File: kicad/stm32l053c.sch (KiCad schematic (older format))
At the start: 29 parts, among them P1 SWD, P2 PWR, Q1 Q_NMOS_GSD, SW1 SW_PUSH, SW2 SW_PUSH, SW3 SW_PUSH, U1 STM32L053C8_LQFP48, U2 TLV61225, Y1 Crystal

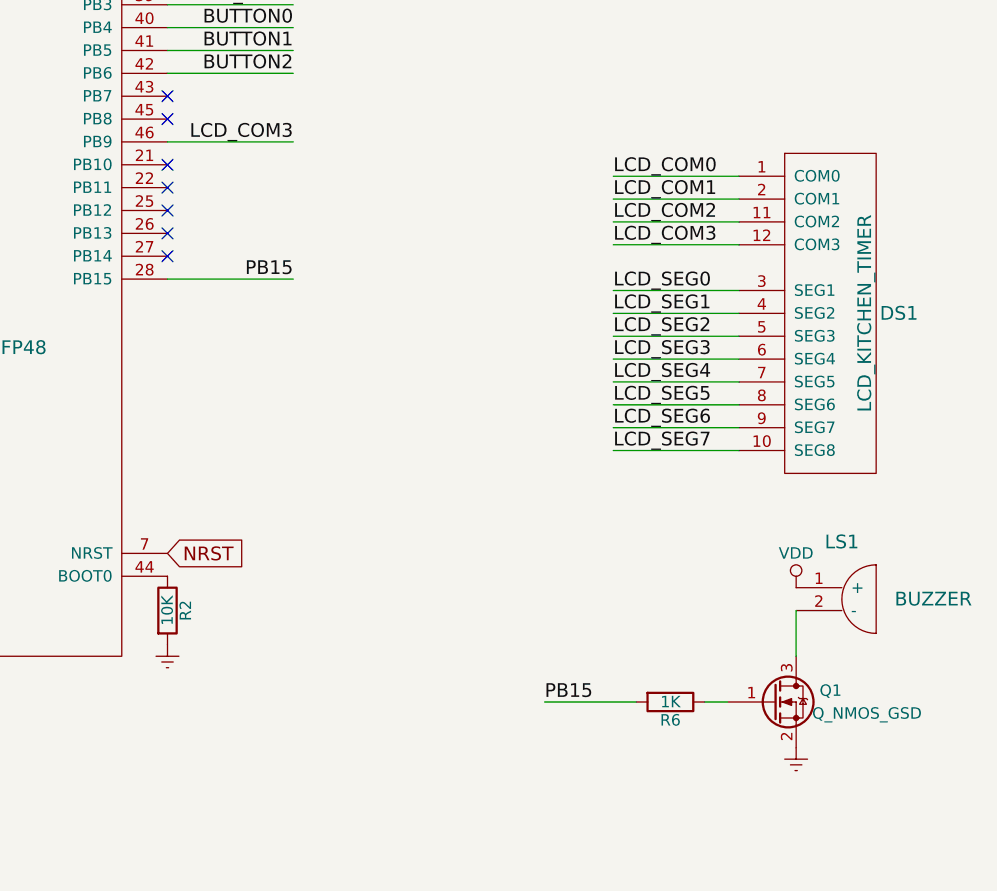
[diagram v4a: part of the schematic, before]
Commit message: 62 ms pulses of 2048Hz for the buzzer alarm
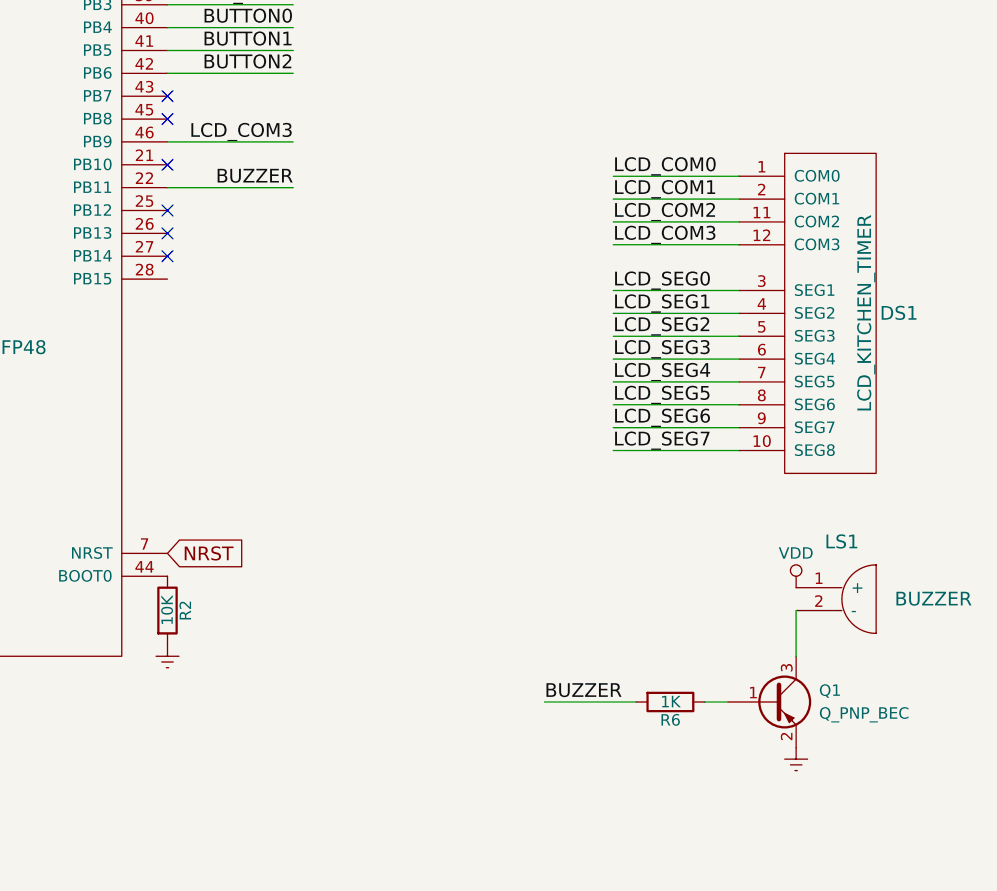
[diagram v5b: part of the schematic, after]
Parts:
- removed Q1: Q_NMOS_GSD, TO_SOT_Packages_SMD:SOT-23_Handsoldering, symbol Q_NMOS_GSD
- added Q1: Q_PNP_BEC, symbol Q_PNP_BEC
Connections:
- net Earth: now also Q1.2 (E)
- net BUZZER: now reaches U1.22 (PB11)
- net BUZZER: now also R6.2
- net at LS1.2 (-): now also Q1.3 (C)
- net at R6.1: now also Q1.1 (B)
- net PB15: no longer names the net of U1.28 (PB15)
- net PB15: no longer R6.2
- no-connect marks 15 -> 14
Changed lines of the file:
@@
 $EndDescr
 $Comp
-L Earth #PWR01
+L Earth #PWR27
 U 1 1 58021BE1
 P 4900 7200
-F 0 "#PWR01" H 4900 6950 50  0001 C CNN
+F 0 "#PWR27" H 4900 6950 50  0001 C CNN
 F 1 "Earth" H 4900 7050 50  0001 C CNN
 F 2 "" H 4900 7200 50  0000 C CNN
@@
 $EndComp
 $Comp
-L VDD #PWR02
+L VDD #PWR25
 U 1 1 58021C2A
 P 4900 6900
-F 0 "#PWR02" H 4900 6750 50  0001 C CNN
+F 0 "#PWR25" H 4900 6750 50  0001 C CNN
 F 1 "VDD" H 4900 7050 50  0000 C CNN
 F 2 "" H 4900 6900 50  0000 C CNN
@@
 $EndComp
 $Comp
-L GNDA #PWR03
+L GNDA #PWR19
 U 1 1 58021F75
 P 5100 6300
-F 0 "#PWR03" H 5100 6050 50  0001 C CNN
+F 0 "#PWR19" H 5100 6050 50  0001 C CNN
 F 1 "GNDA" H 5100 6150 50  0000 C CNN
 F 2 "" H 5100 6300 50  0000 C CNN
@@
 $EndComp
 $Comp
-L Earth #PWR04
+L Earth #PWR20
 U 1 1 58021F89
 P 5600 6300
-F 0 "#PWR04" H 5600 6050 50  0001 C CNN
+F 0 "#PWR20" H 5600 6050 50  0001 C CNN
 F 1 "Earth" H 5600 6150 50  0001 C CNN
 F 2 "" H 5600 6300 50  0000 C CNN
@@
 $EndComp
 $Comp
-L GNDA #PWR05
+L GNDA #PWR16
 U 1 1 58022154
 P 5150 5800
-F 0 "#PWR05" H 5150 5550 50  0001 C CNN
+F 0 "#PWR16" H 5150 5550 50  0001 C CNN
 F 1 "GNDA" H 5150 5650 50  0000 C CNN
 F 2 "" H 5150 5800 50  0000 C CNN
@@
 $EndComp
 $Comp
-L Earth #PWR06
+L Earth #PWR17
 U 1 1 580221FA
 P 5650 5800
-F 0 "#PWR06" H 5650 5550 50  0001 C CNN
+F 0 "#PWR17" H 5650 5550 50  0001 C CNN
 F 1 "Earth" H 5650 5650 50  0001 C CNN
 F 2 "" H 5650 5800 50  0000 C CNN
@@
 $EndComp
 $Comp
-L VDD #PWR07
+L VDD #PWR1
 U 1 1 5802295B
 P 5450 1050
-F 0 "#PWR07" H 5450 900 50  0001 C CNN
+F 0 "#PWR1" H 5450 900 50  0001 C CNN
 F 1 "VDD" H 5450 1200 50  0000 C CNN
 F 2 "" H 5450 1050 50  0000 C CNN
@@
 $EndComp
 $Comp
-L Earth #PWR08
+L Earth #PWR4
 U 1 1 5803310F
 P 4800 1800
-F 0 "#PWR08" H 4800 1550 50  0001 C CNN
+F 0 "#PWR4" H 4800 1550 50  0001 C CNN
 F 1 "Earth" H 4800 1650 50  0001 C CNN
 F 2 "" H 4800 1800 50  0000 C CNN
@@
 $EndComp
 $Comp
-L Earth #PWR09
+L Earth #PWR3
 U 1 1 580369A9
 P 2150 1400
-F 0 "#PWR09" H 2150 1150 50  0001 C CNN
+F 0 "#PWR3" H 2150 1150 50  0001 C CNN
 F 1 "Earth" H 2150 1250 50  0001 C CNN
 F 2 "" H 2150 1400 50  0000 C CNN
@@
 NRST
 $Comp
-L VDD #PWR010
+L VDD #PWR2
 U 1 1 5803734F
 P 1650 1200
-F 0 "#PWR010" H 1650 1050 50  0001 C CNN
+F 0 "#PWR2" H 1650 1050 50  0001 C CNN
 F 1 "VDD" H 1650 1350 50  0000 C CNN
 F 2 "" H 1650 1200 50  0000 C CNN
@@
 $EndComp
 $Comp
-L Earth #PWR011
+L Earth #PWR28
 U 1 1 5803BDC8
 P 5950 7200
-F 0 "#PWR011" H 5950 6950 50  0001 C CNN
+F 0 "#PWR28" H 5950 6950 50  0001 C CNN
 F 1 "Earth" H 5950 7050 50  0001 C CNN
 F 2 "" H 5950 7200 50  0000 C CNN
@@
 $EndComp
 $Comp
-L Earth #PWR012
+L Earth #PWR12
 U 1 1 58065816
 P 6550 5400
-F 0 "#PWR012" H 6550 5150 50  0001 C CNN
+F 0 "#PWR12" H 6550 5150 50  0001 C CNN
 F 1 "Earth" H 6550 5250 50  0001 C CNN
 F 2 "" H 6550 5400 50  0000 C CNN
@@
 $EndComp
 $Comp
-L Earth #PWR013
+L Earth #PWR14
 U 1 1 5806680D
 P 3600 5700
-F 0 "#PWR013" H 3600 5450 50  0001 C CNN
+F 0 "#PWR14" H 3600 5450 50  0001 C CNN
 F 1 "Earth" H 3600 5550 50  0001 C CNN
 F 2 "" H 3600 5700 50  0000 C CNN
@@
 NoConn ~ 6550 3100
 NoConn ~ 6550 3300
-NoConn ~ 6550 3400
 NoConn ~ 6550 3500
 NoConn ~ 6550 3600
@@
 $EndComp
 $Comp
-L +BATT #PWR015
+L +BATT #PWR22
 U 1 1 584F2368
 P 850 6750
-F 0 "#PWR015" H 850 6600 50  0001 C CNN
+F 0 "#PWR22" H 850 6600 50  0001 C CNN
 F 1 "+BATT" H 850 6890 50  0000 C CNN
 F 2 "" H 850 6750 50  0000 C CNN
@@
 Connection ~ 2700 6550
 $Comp
-L Earth #PWR016
+L Earth #PWR24
 U 1 1 584F287E
 P 2850 6850
-F 0 "#PWR016" H 2850 6600 50  0001 C CNN
+F 0 "#PWR24" H 2850 6600 50  0001 C CNN
 F 1 "Earth" H 2850 6700 50  0001 C CNN
 F 2 "" H 2850 6850 50  0000 C CNN
@@
 $EndComp
 $Comp
-L Earth #PWR017
+L Earth #PWR23
 U 1 1 584F28E3
 P 1700 6850
-F 0 "#PWR017" H 1700 6600 50  0001 C CNN
+F 0 "#PWR23" H 1700 6600 50  0001 C CNN
 F 1 "Earth" H 1700 6700 50  0001 C CNN
 F 2 "" H 1700 6850 50  0000 C CNN
@@
 $EndComp
 $Comp
-L Earth #PWR018
+L Earth #PWR26
 U 1 1 584F2924
 P 1250 7050
-F 0 "#PWR018" H 1250 6800 50  0001 C CNN
+F 0 "#PWR26" H 1250 6800 50  0001 C CNN
 F 1 "Earth" H 1250 6900 50  0001 C CNN
 F 2 "" H 1250 7050 50  0000 C CNN
@@
 $EndComp
 $Comp
-L VDD #PWR019
+L VDD #PWR21
 U 1 1 584F2A51
 P 3700 6400
-F 0 "#PWR019" H 3700 6250 50  0001 C CNN
+F 0 "#PWR21" H 3700 6250 50  0001 C CNN
 F 1 "VDD" H 3700 6550 50  0000 C CNN
 F 2 "" H 3700 6400 50  0000 C CNN
@@
 $EndComp
 $Comp
-L VDD #PWR020
+L VDD #PWR5
 U 1 1 585069C3
 P 1300 2700
-F 0 "#PWR020" H 1300 2550 50  0001 C CNN
+F 0 "#PWR5" H 1300 2550 50  0001 C CNN
 F 1 "VDD" H 1300 2850 50  0000 C CNN
 F 2 "" H 1300 2700 50  0000 C CNN
@@
 $EndComp
 $Comp
-L VDD #PWR021
+L VDD #PWR7
 U 1 1 58506BE4
 P 1300 3300
-F 0 "#PWR021" H 1300 3150 50  0001 C CNN
+F 0 "#PWR7" H 1300 3150 50  0001 C CNN
 F 1 "VDD" H 1300 3450 50  0000 C CNN
 F 2 "" H 1300 3300 50  0000 C CNN
@@
 $EndComp
 $Comp
-L VDD #PWR022
+L VDD #PWR9
 U 1 1 58506C86
 P 1300 3900
-F 0 "#PWR022" H 1300 3750 50  0001 C CNN
+F 0 "#PWR9" H 1300 3750 50  0001 C CNN
 F 1 "VDD" H 1300 4050 50  0000 C CNN
 F 2 "" H 1300 3900 50  0000 C CNN
@@
 	2450 2850 3000 2850
 $Comp
-L Earth #PWR023
+L Earth #PWR6
 U 1 1 5851A35F
 P 2450 3150
-F 0 "#PWR023" H 2450 2900 50  0001 C CNN
+F 0 "#PWR6" H 2450 2900 50  0001 C CNN
 F 1 "Earth" H 2450 3000 50  0001 C CNN
 F 2 "" H 2450 3150 50  0000 C CNN
@@
 $EndComp
 $Comp
-L Earth #PWR024
+L Earth #PWR8
 U 1 1 5851A4F4
 P 2450 3750
-F 0 "#PWR024" H 2450 3500 50  0001 C CNN
+F 0 "#PWR8" H 2450 3500 50  0001 C CNN
 F 1 "Earth" H 2450 3600 50  0001 C CNN
 F 2 "" H 2450 3750 50  0000 C CNN
@@
 $EndComp
 $Comp
-L Earth #PWR025
+L Earth #PWR10
 U 1 1 5851A54D
 P 2450 4350
-F 0 "#PWR025" H 2450 4100 50  0001 C CNN
+F 0 "#PWR10" H 2450 4100 50  0001 C CNN
 F 1 "Earth" H 2450 4200 50  0001 C CNN
 F 2 "" H 2450 4350 50  0000 C CNN
@@
 	8600 5650 8200 5650
 $Comp
-L Earth #PWR026
+L Earth #PWR18
 U 1 1 5851B22D
 P 9300 5850
-F 0 "#PWR026" H 9300 5600 50  0001 C CNN
+F 0 "#PWR18" H 9300 5600 50  0001 C CNN
 F 1 "Earth" H 9300 5700 50  0001 C CNN
 F 2 "" H 9300 5850 50  0000 C CNN
@@
 $EndComp
 $Comp
-L VDD #PWR027
+L VDD #PWR11
 U 1 1 5851B377
 P 9300 5150
-F 0 "#PWR027" H 9300 5000 50  0001 C CNN
+F 0 "#PWR11" H 9300 5000 50  0001 C CNN
 F 1 "VDD" H 9300 5300 50  0000 C CNN
 F 2 "" H 9300 5150 50  0000 C CNN
@@
 	1    0    0    -1
 $EndComp
-$Comp
-L Q_NMOS_GSD Q1
-U 1 1 585590EB
-P 9200 5650
-F 0 "Q1" H 9500 5700 50  0000 R CNN
-F 1 "Q_NMOS_GSD" H 9850 5600 50  0000 R CNN
-F 2 "TO_SOT_Packages_SMD:SOT-23_Handsoldering" H 9400 5750 50  0001 C CNN
-F 3 "" H 9200 5650 50  0000 C CNN
-	1    9200 5650
-	1    0    0    -1
-$EndComp
-Text Label 7100 3800 2    60   ~ 0
-PB15
-Wire Wire Line
-	6550 3800 7100 3800
-Text Label 8200 5650 0    60   ~ 0
-PB15
+Text Label 7100 3400 2    60   ~ 0
+BUZZER
 $Comp
 L R R7
@@
 $EndComp
 $Comp
-L +BATT #PWR028
+L +BATT #PWR13
 U 1 1 5857BD0C
 P 1150 5650
-F 0 "#PWR028" H 1150 5500 50  0001 C CNN
+F 0 "#PWR13" H 1150 5500 50  0001 C CNN
 F 1 "+BATT" H 1150 5790 50  0000 C CNN
 F 2 "" H 1150 5650 50  0000 C CNN
@@
 $EndComp
 $Comp
-L Earth #PWR029
+L Earth #PWR15
 U 1 1 5857BE4D
 P 1150 5750
-F 0 "#PWR029" H 1150 5500 50  0001 C CNN
+F 0 "#PWR15" H 1150 5500 50  0001 C CNN
 F 1 "Earth" H 1150 5600 50  0001 C CNN
 F 2 "" H 1150 5750 50  0000 C CNN
@@
 	3500 2100 3900 2100
 Connection ~ 3900 2300
+Wire Wire Line
+	6550 3400 7100 3400
+Text Label 8200 5650 0    60   ~ 0
+BUZZER
+$Comp
+L Q_PNP_BEC Q1
+U 1 1 586901C2
+P 9200 5650
+F 0 "Q1" H 9400 5700 50  0000 L CNN
+F 1 "Q_PNP_BEC" H 9400 5600 50  0000 L CNN
+F 2 "" H 9400 5750 50  0000 C CNN
+F 3 "" H 9200 5650 50  0000 C CNN
+	1    9200 5650
+	1    0    0    -1
+$EndComp
 $EndSCHEMATC

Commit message: STATE_RESET
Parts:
- added R1, R8: 0, Resistors_SMD:R_0805_HandSoldering, symbol R
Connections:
- net BUZZER: now also R1.2; no longer R6.2
- net ALARM: now reaches U1.28 (PB15)
- net ALARM: now also R8.2
- new net: R1.1, R6.2, R8.1
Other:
- moved on the sheet: DS1, LS1, Q1, R6

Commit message: Buzzer or Melody
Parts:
- removed R8: 0, Resistors_SMD:R_0805_HandSoldering, symbol R
- added D1, D2, D3: D_Schottky, Diodes_SMD:D_0805, symbol D_Schottky
- added D4: D, Diodes_SMD:D_0805, symbol D
- added U3: um66t, TO_SOT_Packages_THT:TO-92_Inline_Narrow_Oval, symbol um66t
- Q1: footprint (none) -> TO_SOT_Packages_SMD:SOT-23_Handsoldering
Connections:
- net BUTTON0: now also D1.2 (A); no longer C10.1, C11.1, R4.1, R5.1, U1.10 (PAO), U1.41 (PB5), U1.42 (PB6)
- net Earth: now also U3.3 (VSS)
- net VDD: now also D4.1 (K)
- net at LS1.2 (-), Q1.3 (C): now also D4.2 (A)
- net at R1.1, R6.2: now also U3.1 (OUT)
- net ALARM renamed MELODY
- net MELODY: now also U3.2 (VDD)
- new net BUTTON1: C10.1, D2.2 (A), R4.1, U1.41 (PB5)
- new net BUTTON2: C11.1, D3.2 (A), R5.1, U1.42 (PB6)
- new net WAKEUP_PIN1: D1.1 (K), D2.1 (K), D3.1 (K), U1.10 (PAO)
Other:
- note added: "Either BUZZER or MELODY"
- moved on the sheet: DS1, LS1, R1
